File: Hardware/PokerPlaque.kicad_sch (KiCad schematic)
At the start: 7 parts, among them J1 Conn_01x05_Pin, J2 Conn_01x04_Pin, J3 Conn_01x08_Pin, J4 Conn_01x02_Pin, U2 ATtiny1616-M

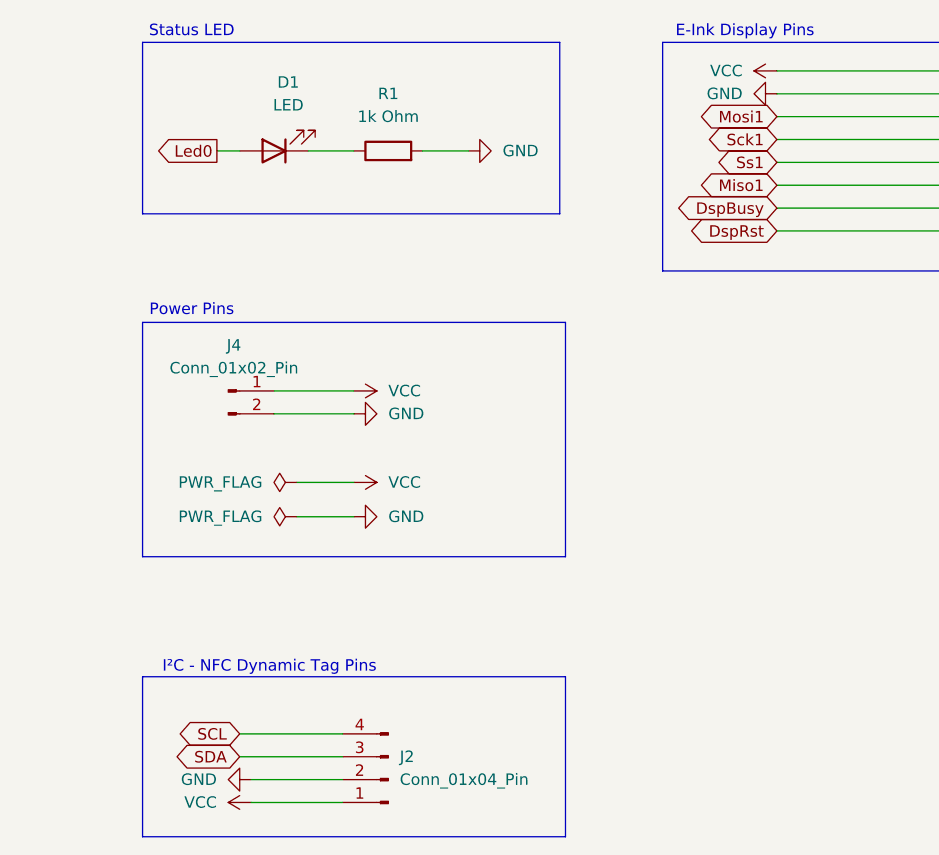
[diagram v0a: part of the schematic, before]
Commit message: I f-ed the whole pcb, here is my rework, rip 50 euros
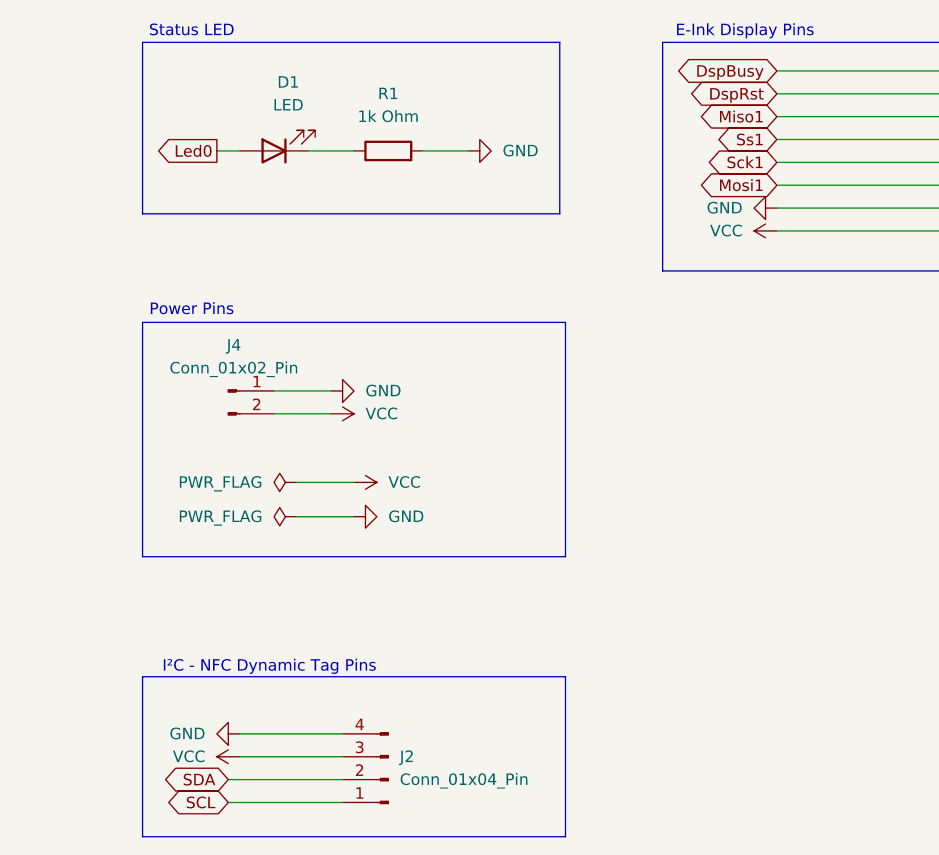
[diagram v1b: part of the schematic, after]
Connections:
- net DspBusy: now also J3.8 (Pin_8); no longer J3.2 (Pin_2)
- net DspRst: now also J3.7 (Pin_7); no longer J3.1 (Pin_1)
- net GND: now also J2.4 (Pin_4), J3.2 (Pin_2), J4.1 (Pin_1); no longer J2.2 (Pin_2), J3.7 (Pin_7), J4.2 (Pin_2)
- net Miso1: now also J3.6 (Pin_6); no longer J3.3 (Pin_3)
- net Mosi1: now also J3.3 (Pin_3); no longer J3.6 (Pin_6)
- net SCL: now also J2.1 (Pin_1); no longer J2.4 (Pin_4)
- net SDA: now also J2.2 (Pin_2); no longer J2.3 (Pin_3)
- net Sck1: now also J3.4 (Pin_4); no longer J3.5 (Pin_5)
- net Ss1: now also J3.5 (Pin_5); no longer J3.4 (Pin_4)
- net VCC: now also J2.3 (Pin_3), J3.1 (Pin_1), J4.2 (Pin_2); no longer J2.1 (Pin_1), J3.8 (Pin_8), J4.1 (Pin_1)
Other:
- company: PokerPassion -> PokerPassion aka Poker-NG
- title: Poker Plaquet Test Board -> Poker Plaque Test Board

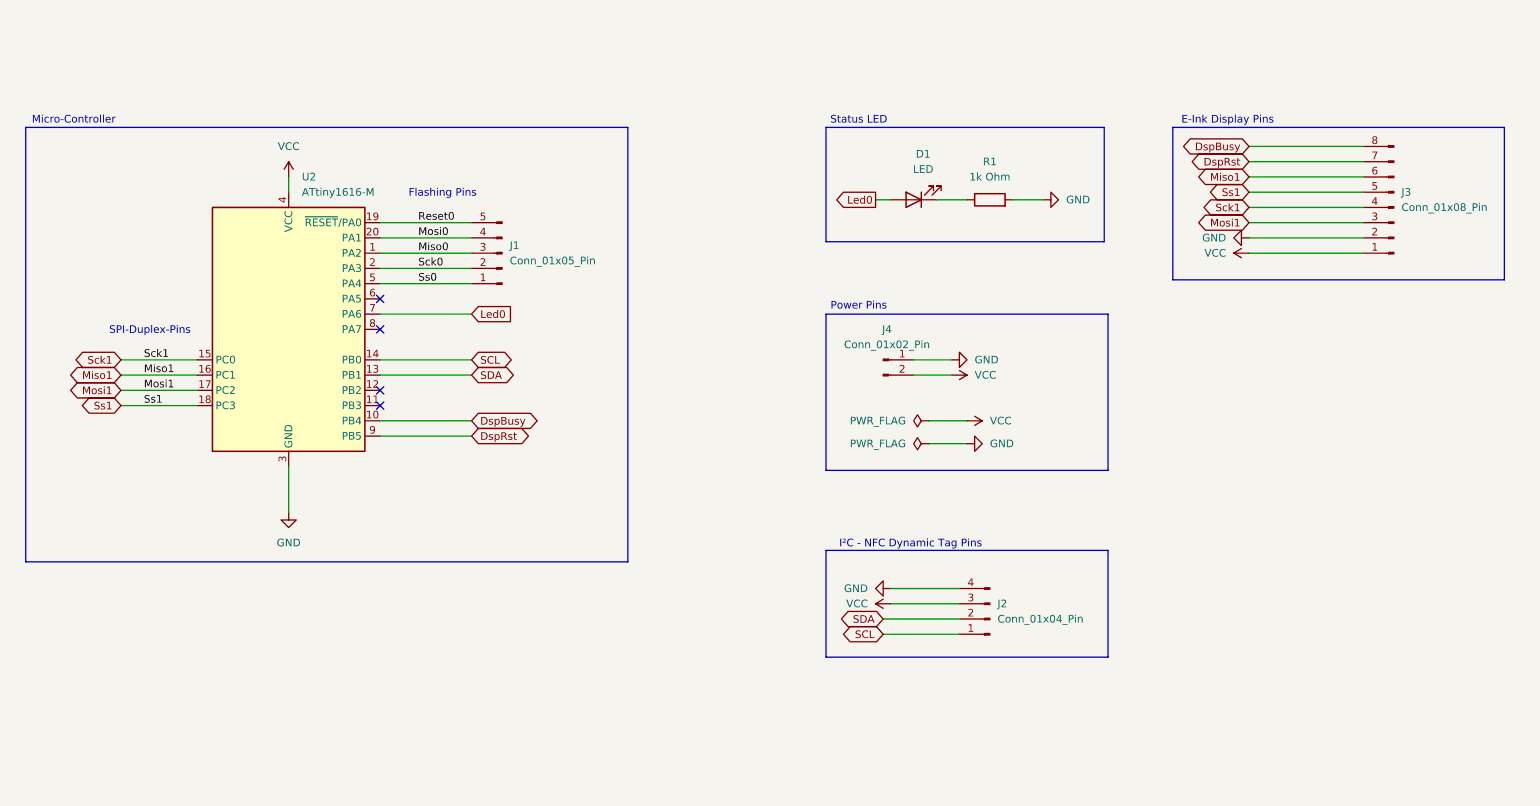
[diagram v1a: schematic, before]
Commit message: feat: new riscv design
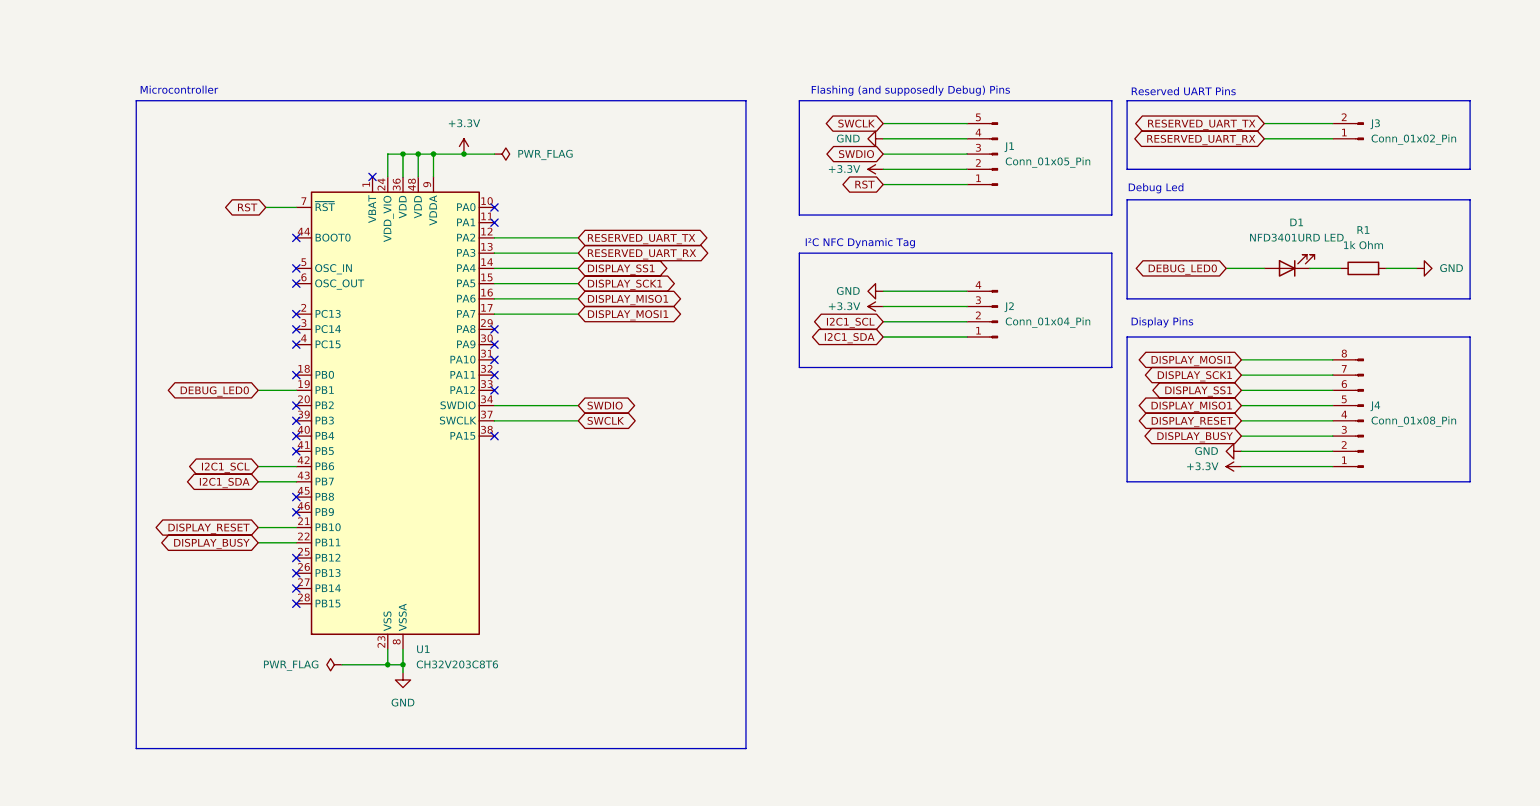
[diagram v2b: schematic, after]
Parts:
- removed J3: Conn_01x08_Pin, Connector_PinHeader_2.54mm:PinHeader_1x08_P2.54mm_Horizontal, symbol Connector:Conn_01x08_Pin
- removed J4: Conn_01x02_Pin, Connector_PinHeader_2.54mm:PinHeader_1x02_P2.54mm_Horizontal, symbol Connector:Conn_01x02_Pin
- removed U2: ATtiny1616-M, Package_DFN_QFN:VQFN-20-1EP_3x3mm_P0.4mm_EP1.7x1.7mm, symbol MCU_Microchip_ATtiny:ATtiny1616-M
- added J3: Conn_01x02_Pin, Connector_PinHeader_2.54mm:PinHeader_1x02_P2.54mm_Horizontal, symbol Connector:Conn_01x02_Pin
- added J4: Conn_01x08_Pin, Connector_PinHeader_2.54mm:PinHeader_1x08_P2.54mm_Horizontal, symbol Connector:Conn_01x08_Pin
- added U1: CH32V203C8T6, Package_QFP:LQFP-48_7x7mm_P0.5mm, symbol MCU_WCH_CH32V2:CH32V203CxTx
- D1: value LED -> NFD3401URD LED; footprint LED_THT:LED_D4.0mm -> LED_THT:LED_D3.0mm
- R1: footprint Resistor_SMD:R_2010_5025Metric -> Resistor_SMD:R_1210_3225Metric
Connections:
- net Mosi0 is gone; now on net GND: J1.4 (Pin_4)
- net VCC is gone; now on net +3.3V: J2.3 (Pin_3)
- net GND: now also J4.2 (Pin_2), U1.23 (VSS), U1.35 (VSS), U1.47 (VSS), U1.8 (VSSA)
- net Led0 renamed DEBUG_LED0
- net DEBUG_LED0: now also U1.19 (PB1)
- net Miso0 renamed SWDIO
- net SWDIO: now also U1.34 (SWDIO)
- net Reset0 renamed SWCLK
- net SWCLK: now also U1.37 (SWCLK)
- net SCL renamed I2C1_SDA
- net I2C1_SDA: now also U1.43 (PB7)
- net SDA renamed I2C1_SCL
- net I2C1_SCL: now also U1.42 (PB6)
- net Sck0 renamed +3.3V
- net +3.3V: now also J4.1 (Pin_1), U1.24 (VDD_VIO), U1.36 (VDD), U1.48 (VDD), U1.9 (VDDA)
- net Ss0 renamed RST
- net RST: now also U1.7 (~{RST})
- new net DISPLAY_BUSY: J4.3 (Pin_3), U1.22 (PB11)
- new net DISPLAY_MISO1: J4.5 (Pin_5), U1.16 (PA6)
- new net DISPLAY_MOSI1: J4.8 (Pin_8), U1.17 (PA7)
- new net DISPLAY_RESET: J4.4 (Pin_4), U1.21 (PB10)
- new net DISPLAY_SCK1: J4.7 (Pin_7), U1.15 (PA5)
- new net DISPLAY_SS1: J4.6 (Pin_6), U1.14 (PA4)
- new net RESERVED_UART_RX: J3.1 (Pin_1), U1.13 (PA3)
- new net RESERVED_UART_TX: J3.2 (Pin_2), U1.12 (PA2)
- no-connect marks 4 -> 26
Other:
- note added: "Debug Led"
- note added: "Display Pins"
- note added: "Flashing (and supposedly Debug) Pins"
- note added: "I²C NFC Dynamic Tag"
- note added: "Microcontroller"
- note added: "Reserved UART Pins"
- note removed: "E-Ink Display Pins"
- note removed: "Flashing Pins"
- note removed: "I²C - NFC Dynamic Tag Pins"
- note removed: "Micro-Controller"
- note removed: "Power Pins"
- note removed: "SPI-Duplex-Pins"
- note removed: "Status LED"
- company: PokerPassion aka Poker-NG -> (none)
- title: Poker Plaque Test Board -> (none)

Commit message: feat: added some necessities
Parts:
- added R2, R3: 10k Ohm, Resistor_SMD:R_1210_3225Metric, symbol Device:R
- added SW1: KH-6X6X6H-STM, Button_Switch_SMD:SW_Push_1P1T_NO_6x6mm_H9.5mm, symbol Switch:SW_Push
- D1: value NFD3401URD LED -> NFD3401URD
- J1: value Conn_01x05_Pin -> A2541WR-5P
- J2: value Conn_01x04_Pin -> A2541WR-4P
- J3: value Conn_01x02_Pin -> A2541WR-2P
- J4: value Conn_01x08_Pin -> A2541WR-8P
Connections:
- net +3.3V: now also U1.1 (VBAT), SW1.2
- net GND: now also R2.1, R3.1
- net BOOT1: now reaches U1.20 (PB2)
- net BOOT1: now also R3.2
- net BOOT0: now reaches U1.44 (BOOT0)
- net BOOT0: now also R2.2, SW1.1
- no-connect marks 26 -> 23
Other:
- note added: "BOOT0/BOOT1"
- company: (none) -> PokerPassion (Poker-NG)
- title: (none) -> Poker Plaque (RISCV)

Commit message: feat: changed some things
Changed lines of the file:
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@@
-	)
-	(junction
-		(at 106.68 43.18)
-		(diameter 0)
-		(color 0 0 0 0)
 	)
 	(junction
@@
 	(wire
 		(pts
-			(xy 106.68 43.18) (xy 111.76 43.18)
-		)
-		(stroke
-			(width 0)
-			(type default)
-		)
-	)
-	(wire
-		(pts
 			(xy 111.76 59.69) (xy 125.73 59.69)
 		)
@@
 		(pts
 			(xy 236.22 92.71) (xy 251.46 92.71)
+		)
+		(stroke
+			(width 0)
+			(type default)
+		)
+	)
+	(wire
+		(pts
+			(xy 128.27 43.18) (xy 138.43 43.18)
 		)
 		(stroke
@@
 				(path "/35fc7dcb-1b02-4664-9231-ed066786cd37"
 					(reference "R2")
+					(unit 1)
+				)
+			)
+		)
+	)
+	(symbol
+		(lib_id "power:PWR_FLAG")
+		(at 138.43 43.18 0)
+		(unit 1)
+		(exclude_from_sim no)
+		(in_bom yes)
+		(on_board yes)
+		(dnp no)
+		(fields_autoplaced yes)
+		(property "Reference" "#FLG02"
+			(at 138.43 41.275 0)
+			(effects
+				(font
+					(size 1.27 1.27)
+				)
+				(hide yes)
+			)
+		)
+		(property "Value" "PWR_FLAG"
+			(at 138.43 38.1 0)
+			(effects
+				(font
+					(size 1.27 1.27)
+				)
+			)
+		)
+		(property "Footprint" ""
+			(at 138.43 43.18 0)
+			(effects
+				(font
+					(size 1.27 1.27)
+				)
+				(hide yes)
+			)
+		)
+		(property "Datasheet" "~"
+			(at 138.43 43.18 0)
+			(effects
+				(font
+					(size 1.27 1.27)
+				)
+				(hide yes)
+			)
+		)
+		(property "Description" "Special symbol for telling ERC where power comes from"
+			(at 138.43 43.18 0)
+			(effects
+				(font
+					(size 1.27 1.27)
+				)
+				(hide yes)
+			)
+		)
+		(pin "1"
+		)
+		(instances
+			(project ""
+				(path "/35fc7dcb-1b02-4664-9231-ed066786cd37"
+					(reference "#FLG02")
 					(unit 1)
 				)
@@
 	)
 	(symbol
-		(lib_id "power:PWR_FLAG")
-		(at 111.76 43.18 270)
-		(unit 1)
-		(exclude_from_sim no)
-		(in_bom yes)
-		(on_board yes)
-		(dnp no)
-		(fields_autoplaced yes)
-		(property "Reference" "#FLG02"
-			(at 113.665 43.18 0)
-			(effects
-				(font
-					(size 1.27 1.27)
-				)
-				(hide yes)
-			)
-		)
-		(property "Value" "PWR_FLAG"
-			(at 115.57 43.1799 90)
-			(effects
-				(font
-					(size 1.27 1.27)
-				)
-				(justify left)
-			)
-		)
-		(property "Footprint" ""
-			(at 111.76 43.18 0)
-			(effects
-				(font
-					(size 1.27 1.27)
-				)
-				(hide yes)
-			)
-		)
-		(property "Datasheet" "~"
-			(at 111.76 43.18 0)
-			(effects
-				(font
-					(size 1.27 1.27)
-				)
-				(hide yes)
-			)
-		)
-		(property "Description" "Special symbol for telling ERC where power comes from"
-			(at 111.76 43.18 0)
-			(effects
-				(font
-					(size 1.27 1.27)
-				)
-				(hide yes)
-			)
-		)
-		(pin "1"
-		)
-		(instances
-			(project ""
-				(path "/35fc7dcb-1b02-4664-9231-ed066786cd37"
-					(reference "#FLG02")
-					(unit 1)
-				)
-			)
-		)
-	)
-	(symbol
 		(lib_id "power:+3.3V")
 		(at 236.22 95.25 90)
@@
 					(unit 1)
 				)
+			)
+		)
+	)
+	(symbol
+		(lib_id "power:+3.3V")
+		(at 128.27 43.18 0)
+		(unit 1)
+		(exclude_from_sim no)
+		(in_bom yes)
+		(on_board yes)
+		(dnp no)
+		(fields_autoplaced yes)
+		(property "Reference" "#PWR013"
+			(at 128.27 46.99 0)
+			(effects
+				(font
+					(size 1.27 1.27)
+				)
+				(hide yes)
+			)
+		)
+		(property "Value" "+3.3V"
+			(at 128.27 38.1 0)
+			(effects
+				(font
+					(size 1.27 1.27)
+				)
+			)
+		)
+		(property "Footprint" ""
+			(at 128.27 43.18 0)
+			(effects
+				(font
+					(size 1.27 1.27)
+				)
+				(hide yes)
+			)
+		)
+		(property "Datasheet" ""
+			(at 128.27 43.18 0)
+			(effects
+				(font
+					(size 1.27 1.27)
+				)
+				(hide yes)
+			)
+		)
+		(property "Description" "Power symbol creates a global label with name \"+3.3V\""
+			(at 128.27 43.18 0)
+			(effects
+				(font
+					(size 1.27 1.27)
+				)
+				(hide yes)
+			)
+		)
+		(pin "1"
+		)
+		(instances
+			(project ""
+				(path "/35fc7dcb-1b02-4664-9231-ed066786cd37"
+					(reference "#PWR013")
+					(unit 1)
+				)

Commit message: feat: more things
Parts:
- added IC1: M24C32-RMN6TP, M24C32-RMN6TP:SOIC127P600X175-8N, symbol M24C32-RMN6TP:M24C32-RMN6TP
- added R4, R5, R6, R7: 1210W2J0103T5E, Resistor_SMD:R_1210_3225Metric, symbol Device:R
- R1: value 1k Ohm -> 1210W2F1001T5E
- R2, R3: value 10k Ohm -> 1210W2J0103T5E
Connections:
- net +3.3V: now also IC1.8 (VCC), R4.2, R5.1, R6.1, R7.1
- net DISPLAY_BUSY: now also J4.8 (Pin_8), U1.46 (PB9); no longer J4.3 (Pin_3), U1.22 (PB11)
- net DISPLAY_MISO1: now also J4.6 (Pin_6); no longer J4.5 (Pin_5)
- net DISPLAY_MOSI1: now also J4.3 (Pin_3); no longer J4.8 (Pin_8)
- net DISPLAY_RESET: now also J4.7 (Pin_7), U1.45 (PB8); no longer J4.4 (Pin_4), U1.21 (PB10)
- net DISPLAY_SCK1: now also J4.4 (Pin_4); no longer J4.7 (Pin_7)
- net DISPLAY_SS1: now also J4.5 (Pin_5); no longer J4.6 (Pin_6)
- net GND: now also IC1.4 (VSS)
- net I2C1_SCL: now also J2.1 (Pin_1), R5.2; no longer J2.2 (Pin_2)
- net I2C1_SDA: now also J2.2 (Pin_2), R4.1; no longer J2.1 (Pin_1)
- net EEPROM_I2C2_WC: now reaches U1.26 (PB13)
- net EEPROM_I2C2_WC: now also IC1.7 (~{WC})
- net EEPROM_E0: now reaches U1.27 (PB14)
- net EEPROM_E0: now also IC1.1 (E0)
- net EEPROM_E1: now reaches U1.28 (PB15)
- net EEPROM_E1: now also IC1.2 (E1)
- net EEPROM_E2: now reaches U1.38 (PA15)
- net EEPROM_E2: now also IC1.3 (E2)
- new net EEPROM_I2C2_SCL: IC1.6 (SCL), R7.2, U1.21 (PB10)
- new net EEPROM_I2C2_SDA: IC1.5 (SDA), R6.2, U1.22 (PB11)
- no-connect marks 23 -> 17
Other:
- note added: "EEPROM / NVRAM"
- moved on the sheet: D1, R2, R3, SW1
